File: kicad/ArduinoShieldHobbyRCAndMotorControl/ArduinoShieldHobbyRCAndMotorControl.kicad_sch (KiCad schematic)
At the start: 14 parts, among them J1 Power, J2 Digital/PWM, J3 Analog, J4 Digital/PWM

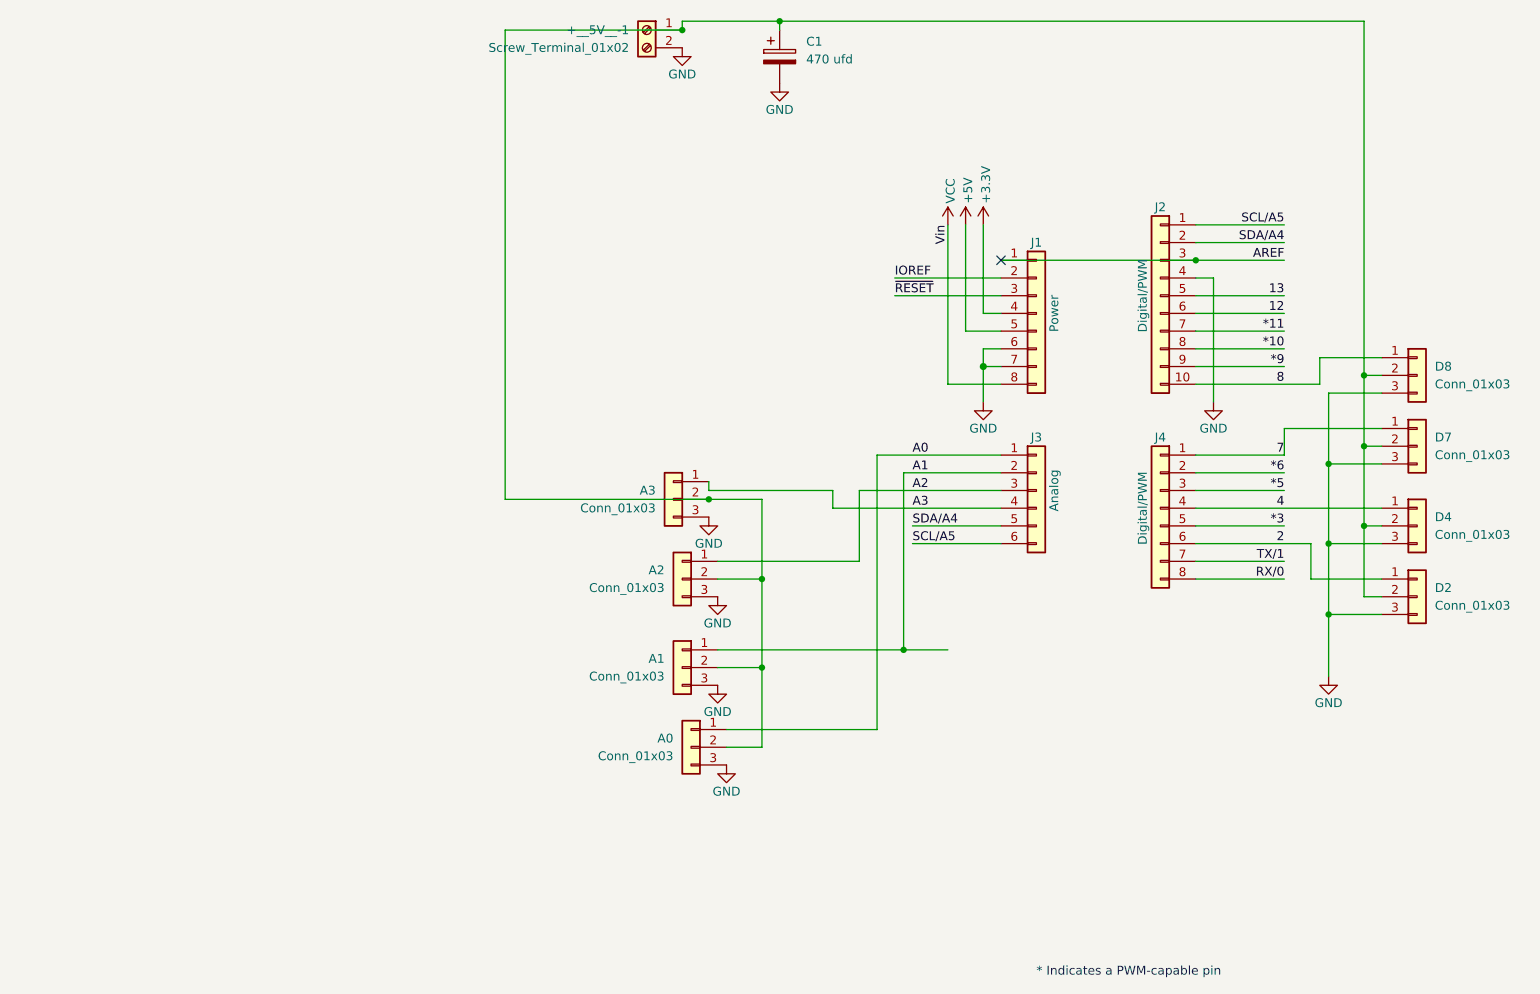
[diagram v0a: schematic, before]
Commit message: finished hobby rc and motor controller shield
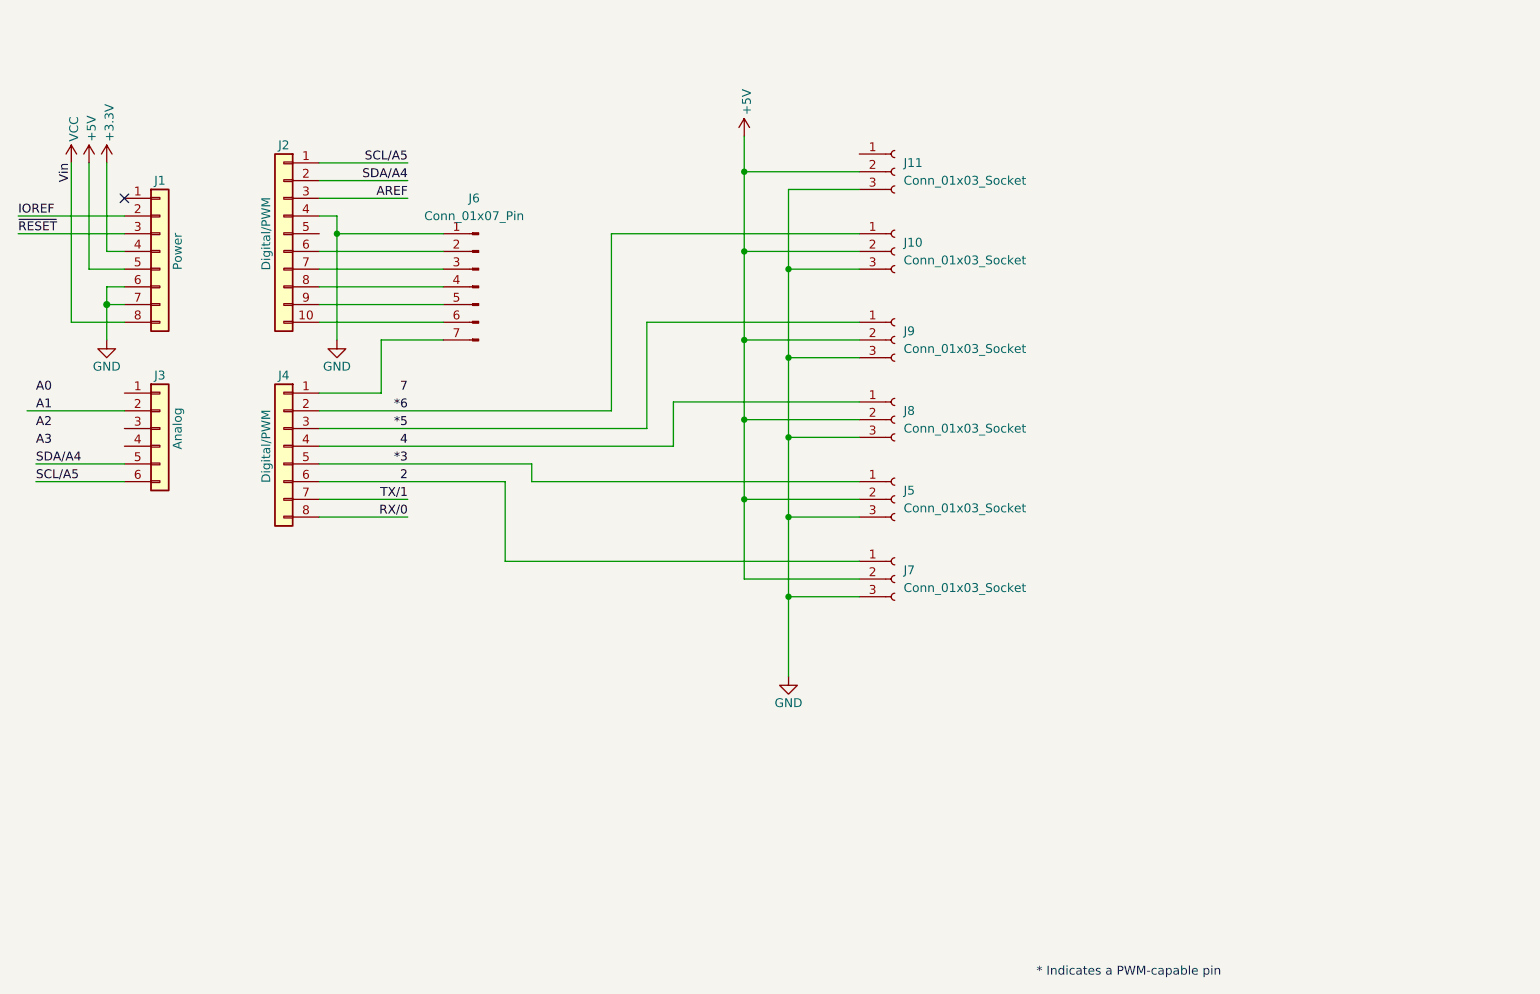
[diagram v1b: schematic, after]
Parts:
- removed +__5V__-1: Screw_Terminal_01x02, TerminalBlock:TerminalBlock_bornier-2_P5.08mm, symbol Connector:Screw_Terminal_01x02
- removed A0, A1, A2, A3, D2, D4, D7, D8: Conn_01x03, Connector_PinHeader_2.54mm:PinHeader_1x03_P2.54mm_Vertical, symbol Connector_Generic:Conn_01x03
- removed C1: 470 ufd, Capacitor_THT:CP_Radial_D10.0mm_P5.00mm, symbol Device:C_Polarized
- added J10, J11, J5, J7, J8, J9: Conn_01x03_Socket, Connector_PinSocket_2.54mm:PinSocket_1x03_P2.54mm_Vertical, symbol Connector:Conn_01x03_Socket
- added J6: Conn_01x07_Pin, Connector_PinHeader_2.54mm:PinHeader_1x07_P2.54mm_Vertical, symbol Connector:Conn_01x07_Pin
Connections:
- net *3: now also J5.1 (Pin_1)
- net *5: now also J9.1 (Pin_1)
- net *6: now also J10.1 (Pin_1)
- net +5V: now also J10.2 (Pin_2), J11.2 (Pin_2), J5.2 (Pin_2), J7.2 (Pin_2), J8.2 (Pin_2), J9.2 (Pin_2)
- net 2: now also J7.1 (Pin_1)
- net 4: now also J8.1 (Pin_1)
- net 7: no longer J4.1 (Pin_1)
- net A0: no longer J3.1 (Pin_1)
- net A2: no longer J3.3 (Pin_3)
- net A3: no longer J3.4 (Pin_4)
- net AREF: no longer J1.1 (Pin_1)
- net GND: now also J10.3 (Pin_3), J11.3 (Pin_3), J5.3 (Pin_3), J6.1 (Pin_1), J7.3 (Pin_3), J8.3 (Pin_3), J9.3 (Pin_3)
- net *10: no longer names the net of J2.8 (Pin_8)
- net *10: now also J6.4 (Pin_4)
- net *11: no longer names the net of J2.7 (Pin_7)
- net *11: now also J6.3 (Pin_3)
- net *9: no longer names the net of J2.9 (Pin_9)
- net *9: now also J6.5 (Pin_5)
- net 12: no longer names the net of J2.6 (Pin_6)
- net 12: now also J6.2 (Pin_2)
- net 13: no longer names the net of J2.5 (Pin_5)
- net 8: no longer names the net of J2.10 (Pin_10)
- net 8: now also J6.6 (Pin_6)
- new net: J4.1 (Pin_1), J6.7 (Pin_7)
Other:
- moved on the sheet: J1, J2, J3, J4

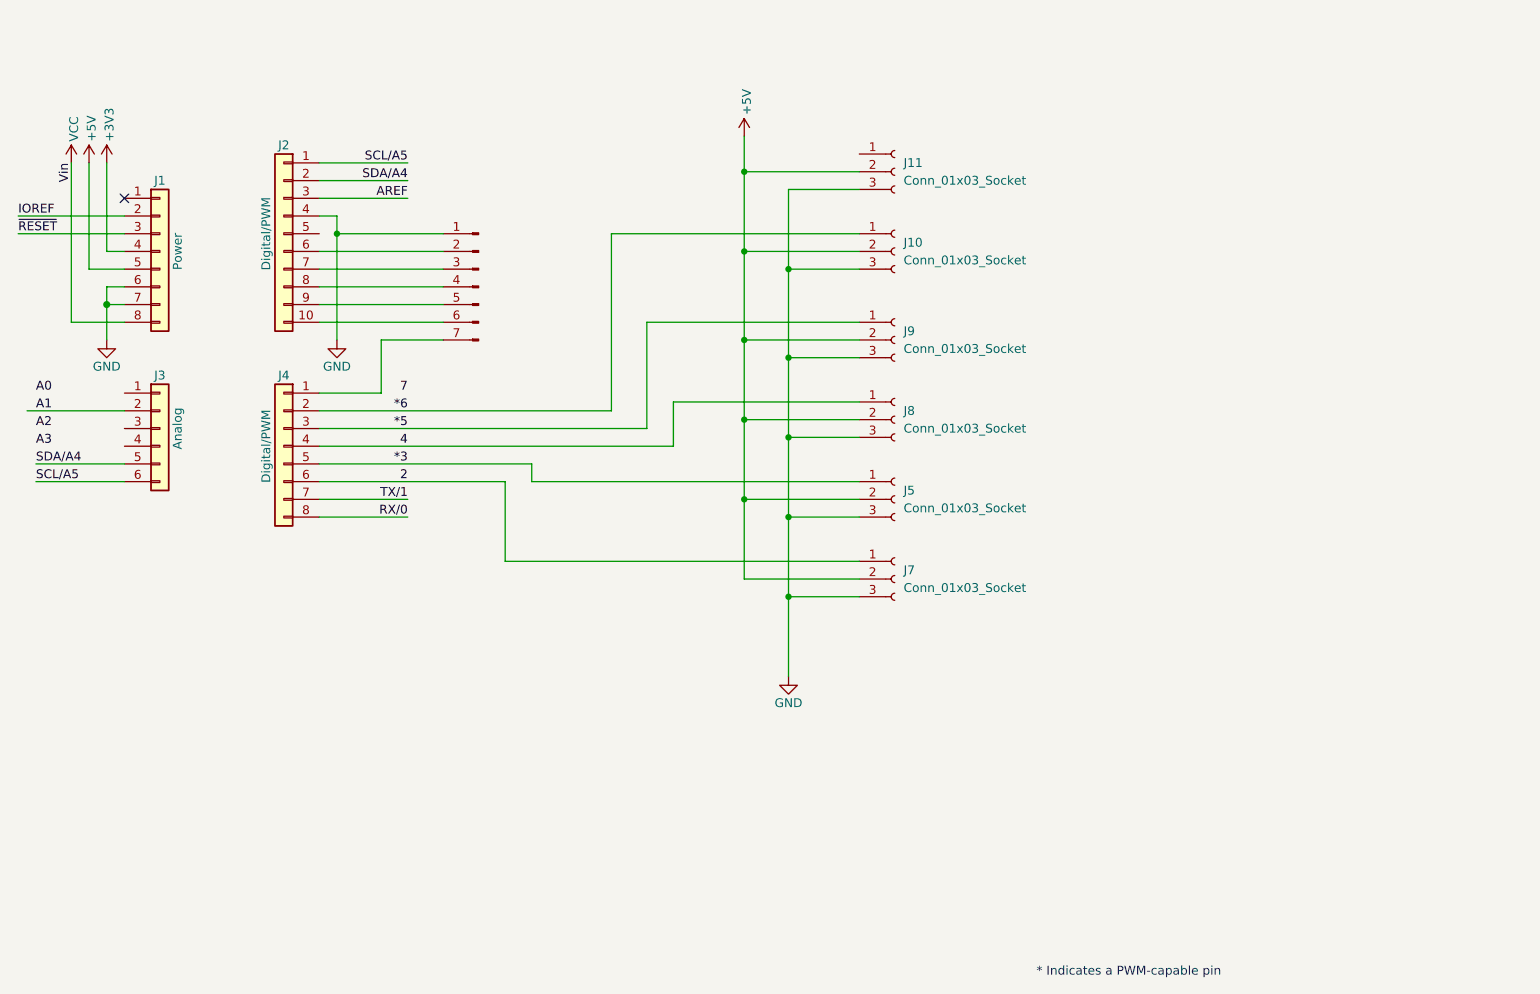
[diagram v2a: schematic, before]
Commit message: rev 2 of arduino shield hobby rc and motor control
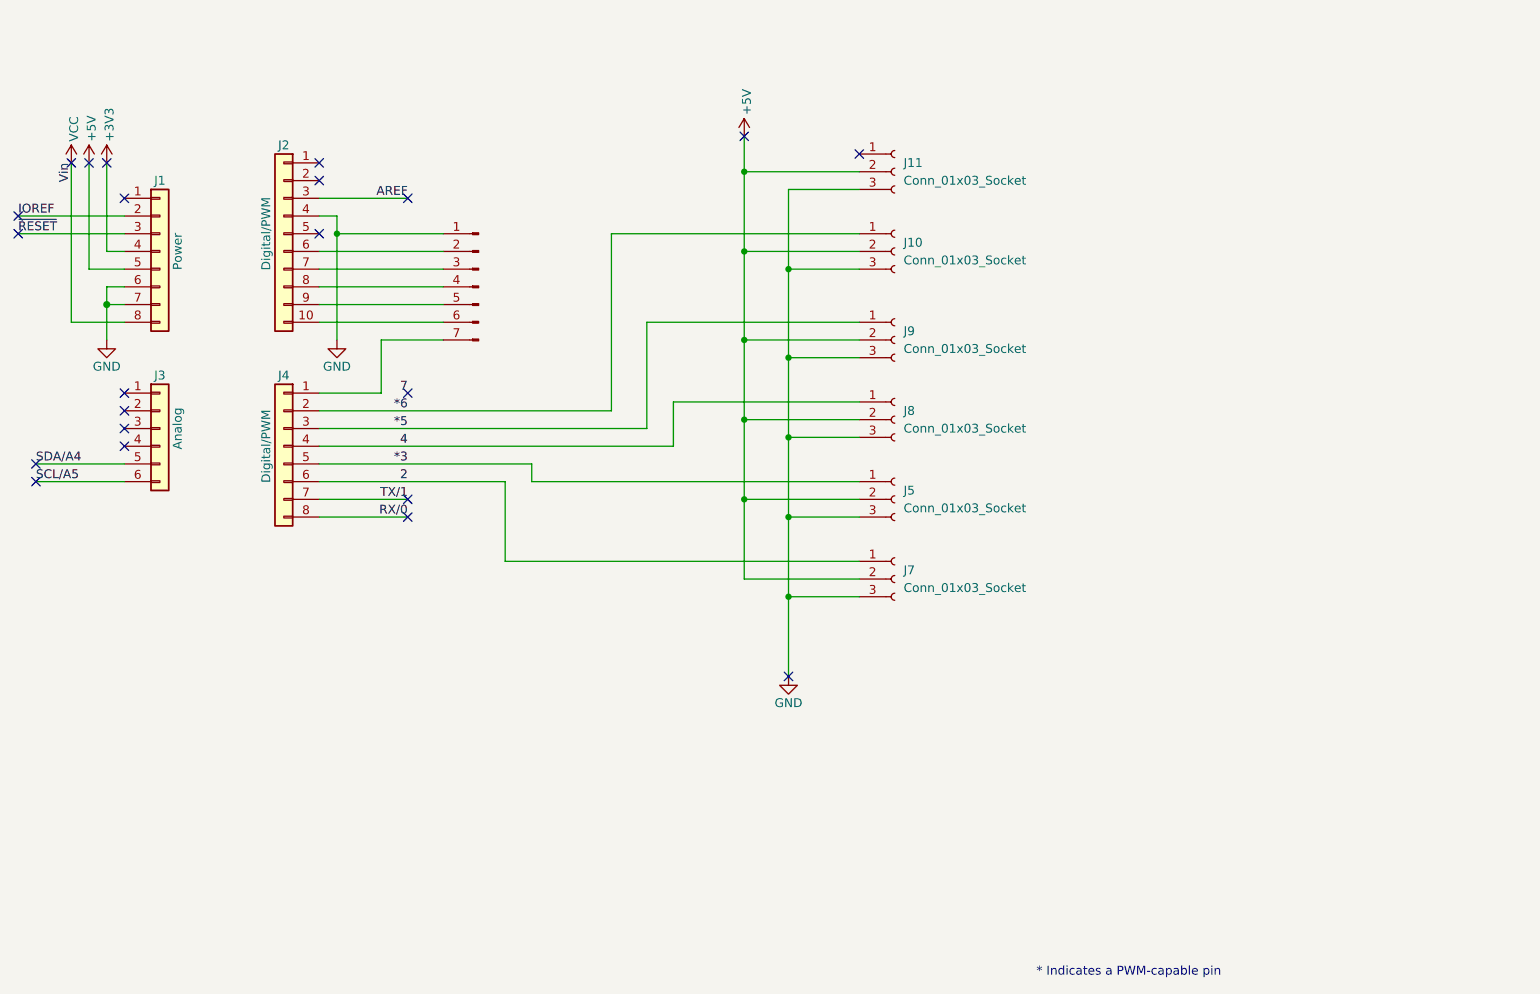
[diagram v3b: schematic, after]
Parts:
- J6: footprint Connector_PinHeader_2.54mm:PinHeader_1x07_P2.54mm_Vertical -> TerminalBlock_WAGO:TerminalBlock_WAGO_236-107_1x07_P5.00mm_45Degree
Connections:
- net SCL/A5: no longer J2.1 (Pin_1)
- net SDA/A4: no longer J2.2 (Pin_2)
- net A1: no longer names the net of J3.2 (Pin_2)
- no-connect marks 1 -> 22
